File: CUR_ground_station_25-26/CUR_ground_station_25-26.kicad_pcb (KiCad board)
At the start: 2 copper layers, 27 parts, among them J2 UJ20-C-H-G-SMT-P16-TR, Q2 NTR4003N, U1 ESP32-S3-WROOM-1, U2 BQ24232RGT, U3 NCP186AMX330TAG, U4 USBLC6-2SC6, U5 E22-400MM_22S, U6 2.13" Epaper Module

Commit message: started layout-ing
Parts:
- removed D1: CLV1L-FKB-CJQRNQEFGBB79353, LED_SMD:LED_Cree-PLCC4_3.2x2.8mm_CCW
- added BZ1: CMT-1209-390T, Buzzer_SameSky:Buzzer_SameSky_CEM-1203_42, F.Cu at (91.3, 61.9)
- added C1: 10u, Capacitor_SMD:C_0603_1608Metric, F.Cu at (140.7, 89.4)
- added C10: 100n, Capacitor_SMD:C_0603_1608Metric, F.Cu at (55.7, 98.1)
- added C11: 100n, Capacitor_SMD:C_0603_1608Metric, F.Cu at (89.5, 98.6)
- added C12: 22u, Capacitor_SMD:C_0603_1608Metric, F.Cu at (89.4, 95.0)
- added C13: 1u, Capacitor_SMD:C_0603_1608Metric, F.Cu at (66.1, 100.3)
- added C14: DNP, Capacitor_SMD:C_0603_1608Metric, F.Cu at (74.9, 85.3)
- added C15: DNP, Capacitor_SMD:C_0603_1608Metric, F.Cu at (75.2, 82.2)
- added C2: 10u, Capacitor_SMD:C_0603_1608Metric, F.Cu at (97.5, 77.3)
- added C3: 10u, Capacitor_SMD:C_0603_1608Metric, F.Cu at (92.9, 77.2)
- added C4: 10u, Capacitor_SMD:C_0603_1608Metric, F.Cu at (101.6, 88.4)
- added C5: 10u, Capacitor_SMD:C_0603_1608Metric, F.Cu at (101.6, 90.9)
- added J1: Conn_01x02, Connector_JST:JST_PH_B2B-PH-K_1x02_P2.00mm_Vertical, F.Cu at (130.1, 97.7)
- added J3: Conn_Coaxial_Small, Conn_Coaxial_RFSOLUTIONS_CON-SMA-EDGE-S:Conn_Coaxial_RFSOLUTIONS_CON-SMA-EDGE-S, F.Cu at (98.2, 30.5)
- added J4: Conn_01x04_Pin, Connector_PinHeader_2.54mm:PinHeader_1x04_P2.54mm_Vertical, F.Cu at (48.3, 91.5)
- added Q1: NTR4003N, Package_TO_SOT_SMD:SOT-23, F.Cu at (100.5, 57.0)
- added R12: 10k, Resistor_SMD:R_0603_1608Metric, F.Cu at (134.9, 88.9)
- added R13: RC0603FR-071K74L, Resistor_SMD:R_0603_1608Metric, F.Cu at (100.0, 73.2)
- added R14: 10k, Resistor_SMD:R_0603_1608Metric, F.Cu at (105.6, 83.4)
- added R15: 35k, Resistor_SMD:R_0603_1608Metric, F.Cu at (105.6, 85.9)
- added R26: 0, Resistor_SMD:R_0603_1608Metric, F.Cu at (62.3, 101.7)
- added R27: 10k, Resistor_SMD:R_0603_1608Metric, F.Cu at (64.2, 100.3)
- added R28: 0, Resistor_SMD:R_0603_1608Metric, F.Cu at (78.9, 82.8)
- added R29: 0, Resistor_SMD:R_0603_1608Metric, F.Cu at (78.9, 85.3)
- added R33: 270, Resistor_SMD:R_0603_1608Metric, F.Cu at (46.5, 61.1)
- added R34: 47, Resistor_SMD:R_0603_1608Metric, F.Cu at (49.9, 61.1)
- added R35: 47, Resistor_SMD:R_0603_1608Metric, F.Cu at (50.6, 58.4)
- added R36: 270, Resistor_SMD:R_0603_1608Metric, F.Cu at (55.6, 61.1)
- added R37: 47, Resistor_SMD:R_0603_1608Metric, F.Cu at (59.0, 61.1)
- added R38: 47, Resistor_SMD:R_0603_1608Metric, F.Cu at (59.8, 58.3)
- added R4: 10k, Resistor_SMD:R_0603_1608Metric, F.Cu at (100.6, 61.5)
- added R5: 150, Resistor_SMD:R_0603_1608Metric, F.Cu at (100.1, 65.2)
- added SW1: PTS815SJM250SMTRLFS, PTS815_SJM_250_SMTR_LFS:SW_Push_PTS815_SJM_250_SMTR_LFS, F.Cu at (49.8, 76.1)
- added SW2: PTS815SJM250SMTRLFS, PTS815_SJM_250_SMTR_LFS:SW_Push_PTS815_SJM_250_SMTR_LFS, F.Cu at (56.3, 81.0)
- added SW3: PTS815SJM250SMTRLFS, PTS815_SJM_250_SMTR_LFS:SW_Push_PTS815_SJM_250_SMTR_LFS, F.Cu at (56.3, 70.7)
- added SW4: PTS815SJM250SMTRLFS, PTS815_SJM_250_SMTR_LFS:SW_Push_PTS815_SJM_250_SMTR_LFS, F.Cu at (62.6, 76.0)
- added SW5: PTS815SJM250SMTRLFS, PTS815_SJM_250_SMTR_LFS:SW_Push_PTS815_SJM_250_SMTR_LFS, F.Cu at (113.9, 110.7)
- added SW7: PTS815SJM250SMTRLFS, PTS815_SJM_250_SMTR_LFS:SW_Push_PTS815_SJM_250_SMTR_LFS, F.Cu at (96.5, 99.4)
- added SW8: PTS815SJM250SMTRLFS, PTS815_SJM_250_SMTR_LFS:SW_Push_PTS815_SJM_250_SMTR_LFS, F.Cu at (59.9, 98.1)
- added TP1: TestPoint_Small, TestPoint_KOASpeer:TestPoint_Chip_RCUCTE_0603, F.Cu at (89.1, 45.2)
- added TP10: TestPoint_Small, TestPoint_KOASpeer:TestPoint_Chip_RCUCTE_0603, F.Cu at (82.0, 42.7)
- added TP11: TestPoint_Small, TestPoint_KOASpeer:TestPoint_Chip_RCUCTE_0603, F.Cu at (82.0, 40.1)
- added TP12: TestPoint_Small, TestPoint_KOASpeer:TestPoint_Chip_RCUCTE_0603, F.Cu at (111.6, 95.1)
- added TP14: TestPoint_Small, TestPoint_KOASpeer:TestPoint_Chip_RCUCTE_0603, F.Cu at (111.6, 97.7)
- added TP15: TestPoint_Small, TestPoint_KOASpeer:TestPoint_Chip_RCUCTE_0603, F.Cu at (111.6, 100.2)
- added TP16: TestPoint_Small, TestPoint_KOASpeer:TestPoint_Chip_RCUCTE_0603, F.Cu at (111.6, 102.8)
- added TP17: TestPoint_Small, TestPoint_KOASpeer:TestPoint_Chip_RCUCTE_0603, F.Cu at (111.6, 105.3)
- added TP2: TestPoint_Small, TestPoint_KOASpeer:TestPoint_Chip_RCUCTE_0603, F.Cu at (89.1, 42.7)
- added TP3: TestPoint_Small, TestPoint_KOASpeer:TestPoint_Chip_RCUCTE_0603, F.Cu at (89.1, 40.1)
- added TP4: TestPoint_Small, TestPoint_KOASpeer:TestPoint_Chip_RCUCTE_0603, F.Cu at (89.1, 37.6)
- added TP5: TestPoint_Small, TestPoint_KOASpeer:TestPoint_Chip_RCUCTE_0603, F.Cu at (85.5, 45.2)
- added TP6: TestPoint_Small, TestPoint_KOASpeer:TestPoint_Chip_RCUCTE_0603, F.Cu at (85.5, 42.7)
- added TP7: TestPoint_Small, TestPoint_KOASpeer:TestPoint_Chip_RCUCTE_0603, F.Cu at (85.5, 40.1)
- added TP8: TestPoint_Small, TestPoint_KOASpeer:TestPoint_Chip_RCUCTE_0603, F.Cu at (85.5, 37.6)
- added TP9: TestPoint_Small, TestPoint_KOASpeer:TestPoint_Chip_RCUCTE_0603, F.Cu at (82.0, 45.2)
- R16, R17, R18, R19: footprint Resistor_SMD:R_0402_1005Metric -> Resistor_SMD:R_0603_1608Metric
- U1: value ESP32-S3-WROOM-1 -> ESP32-S3-MINI-1; footprint RF_Module:ESP32-S3-WROOM-1 -> RF_Module:ESP32-S2-MINI-1
- U3: footprint Package_DFN_QFN:DFN-6-1EP_1.2x1.2mm_P0.4mm_EP0.3x0.94mm_PullBack -> XDFN8_1P6X1P2_onsemi:XDFN8_1P6X1P2_onsemi
- moved U5 77.1 mm to (97.3, 40.0), turned to 180 degrees
- moved R25 64.8 mm to (105.9, 32.7), turned to 180 degrees
- moved R24 59.8 mm to (105.9, 35.2), turned to 180 degrees
- moved R23 54.8 mm to (105.9, 37.7), turned to 180 degrees
- moved C9 49.8 mm to (105.9, 40.2), turned to 180 degrees
- moved C8 44.8 mm to (105.9, 42.7), turned to 180 degrees
- moved D5 42.6 mm to (104.3, 61.3), turned to 180 degrees
- moved C6 39.8 mm to (105.9, 45.2), turned to 180 degrees
- moved Q2 31.1 mm to (107.4, 105.5)
- moved D4 31.0 mm to (107.4, 100.9)
- moved D2 30.8 mm to (107.4, 96.2)
- moved R18 28.0 mm to (120.1, 104.6)
- moved R17 27.5 mm to (120.1, 102.1)
- moved R16 27.0 mm to (120.1, 99.6)
- moved C7 20.9 mm to (114.8, 98.0)
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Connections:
- Q2 pad 3: /Power/PWR_BTN -> /MCU/PWR_BTN
- R17 pad 1: /Power/PWR_EN -> /MCU/PWR_EN
- R23 pad 2: /Telemetry/~{RF_NSS} -> /MCU/~{RF_NSS}
- R24 pad 1: /Telemetry/RF_TXEN -> /MCU/RF_TXEN
- R24 pad 2: /Telemetry/RF_IO2 -> /MCU/RF_IO2
- U1 pad 10: /MCU/RF_IO2 -> /MCU/BUZZER
- U1 pad 12: /MCU/RF_IO3 -> /MCU/RF_IO2
- U1 pad 13: Net-(U1-USB_D-) -> /MCU/RF_IO3
- U1 pad 14: Net-(U1-USB_D+) -> /MCU/~{RF_NSS}
- U1 pad 15: unconnected-(U1-IO3-Pad15) -> /MCU/RF_MOSI
- U1 pad 16: unconnected-(U1-IO46-Pad16) -> /MCU/RF_SCK
- U1 pad 17: unconnected-(U1-IO9-Pad17) -> /MCU/RF_MISO
- U1 pad 18: /MCU/~{RF_NSS} -> /MCU/RF_BUSY
- U1 pad 19: /MCU/RF_MOSI -> /MCU/~{RF_RESET}
- U1 pad 2: +3V3 -> GND
- U1 pad 20: /MCU/RF_SCK -> /MCU/LED_1_R
- U1 pad 21: /MCU/RF_MISO -> /MCU/LED_1_G
- U1 pad 22: /MCU/RF_BUSY -> /MCU/LED_1_B
- U1 pad 23: /MCU/RF_RXEN -> Net-(U1-USB_D-)
- U1 pad 24: unconnected-(U1-IO47-Pad24) -> Net-(U1-USB_D+)
- U1 pad 25: unconnected-(U1-IO48-Pad25) -> /MCU/RF_RXEN
- U1 pad 27: /MCU/BOOT -> /MCU/BTN_3
- U1 pad 28: unconnected-(U1-IO35-Pad28) -> /MCU/LED_2_R
- U1 pad 29: unconnected-(U1-IO36-Pad29) -> /MCU/LED_2_G
- U1 pad 3: /MCU/EN -> +3V3
- U1 pad 30: unconnected-(U1-IO37-Pad30) -> /MCU/BTN_4
- U1 pad 31: unconnected-(U1-IO38-Pad31) -> /MCU/LED_2_B
- U1 pad 32: unconnected-(U1-IO39-Pad32) -> /MCU/DISP_D/~{C}
- U1 pad 33: unconnected-(U1-IO40-Pad33) -> /MCU/DISP_CS
- U1 pad 34: unconnected-(U1-IO41-Pad34) -> /MCU/DISP_SCL
- U1 pad 35: unconnected-(U1-IO42-Pad35) -> /MCU/DISP_SDA
- U1 pad 36: /MCU/UART_RX -> /MCU/DISP_BUSY
- U1 pad 37: /MCU/UART_TX -> /MCU/DISP_~{RES}
- U1 pad 38: unconnected-(U1-IO2-Pad38) -> /MCU/BTN_1
- U1 pad 39: unconnected-(U1-IO1-Pad39) -> /MCU/UART_TX
- U1 pad 4: /MCU/DISP_D/~{C} -> /MCU/BOOT
- U1 pad 40: GND -> /MCU/UART_RX
- U1 pad 41: GND -> /MCU/BTN_2
- U1 pad 5: /MCU/DISP_CS -> /MCU/~{CHG}
- U1 pad 6: /MCU/DISP_SCL -> /MCU/~{PGOOD}
- U1 pad 7: /MCU/DISP_SDA -> /MCU/BATT_VSENSE
- U1 pad 8: /MCU/DISP_~{RES} -> /MCU/PWR_EN
- U1 pad 9: /MCU/~{RF_RESET} -> /MCU/PWR_BTN
- U2 pad 7: /Power/~{PGOOD} -> /MCU/~{PGOOD}
- U2 pad 9: /Power/~{CHG} -> /MCU/~{CHG}
- U4 pad 4: /Power/USB_D+ -> /MCU/USB_D+
- U4 pad 6: /Power/USB_D- -> /MCU/USB_D-
- U5 pad 10: /Telemetry/RF_RXEN -> /MCU/RF_RXEN
- U5 pad 11: /Telemetry/RF_BUSY -> /MCU/RF_BUSY
- U5 pad 12: /Telemetry/RF_MISO -> /MCU/RF_MISO
- U5 pad 13: /Telemetry/RF_MOSI -> /MCU/RF_MOSI
- U5 pad 14: /Telemetry/~{RF_NSS} -> /MCU/~{RF_NSS}
- U5 pad 15: /Telemetry/RF_SCK -> /MCU/RF_SCK
- U5 pad 18: /Telemetry/RF_IO1 -> /MCU/RF_IO1
- U5 pad 19: /Telemetry/RF_IO2 -> /MCU/RF_IO2
- U5 pad 20: /Telemetry/RF_IO3 -> /MCU/RF_IO3
- U5 pad 3: /Telemetry/~{RF_RESET} -> /MCU/~{RF_RESET}
- U5 pad 9: /Telemetry/RF_TXEN -> /MCU/RF_TXEN
- U6 pad 1: /User Interface/DISP_BUSY -> /MCU/DISP_BUSY
- U6 pad 2: /User Interface/DISP_~{RES} -> /MCU/DISP_~{RES}
- U6 pad 3: /User Interface/DISP_D/~{C} -> /MCU/DISP_D/~{C}
- U6 pad 4: /User Interface/DISP_CS -> /MCU/DISP_CS
- U6 pad 5: /User Interface/DISP_SCL -> /MCU/DISP_SCL
- U6 pad 6: /User Interface/DISP_SDA -> /MCU/DISP_SDA

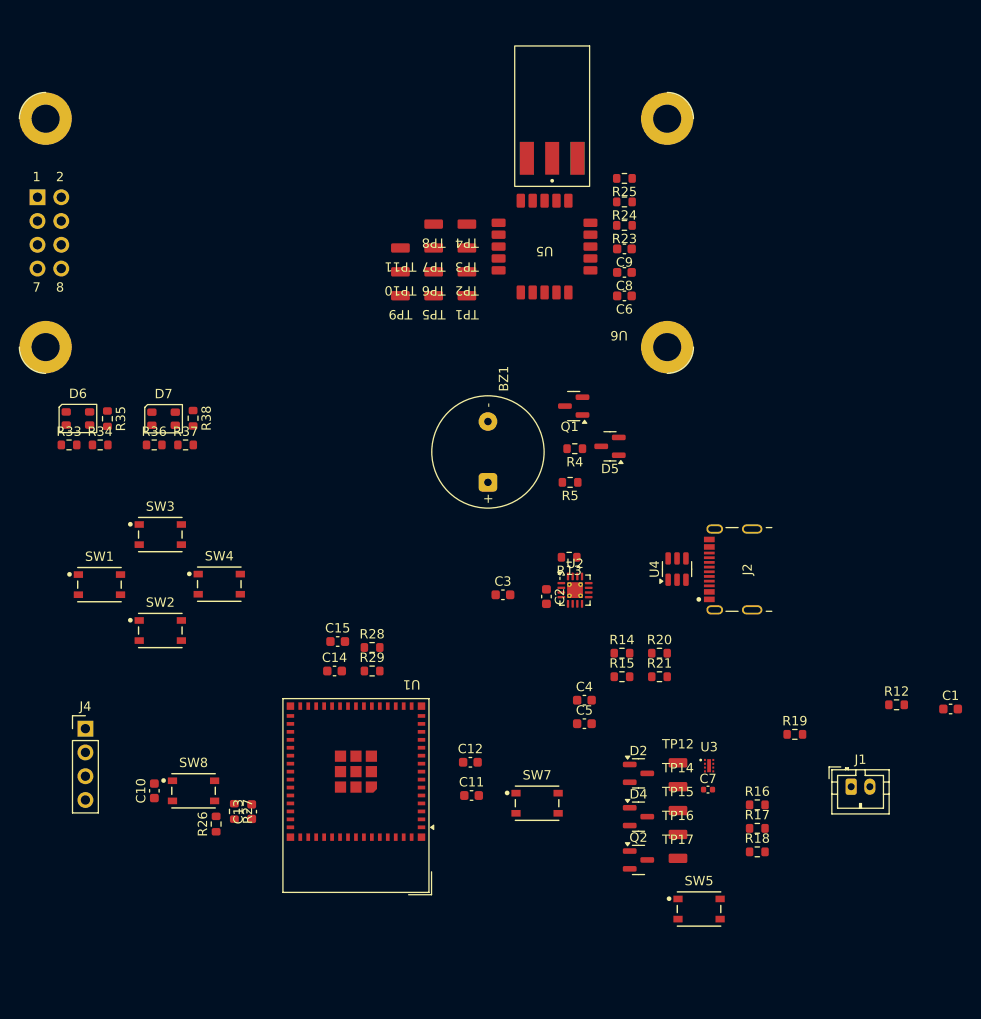
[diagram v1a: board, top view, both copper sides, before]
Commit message: preliminary layout
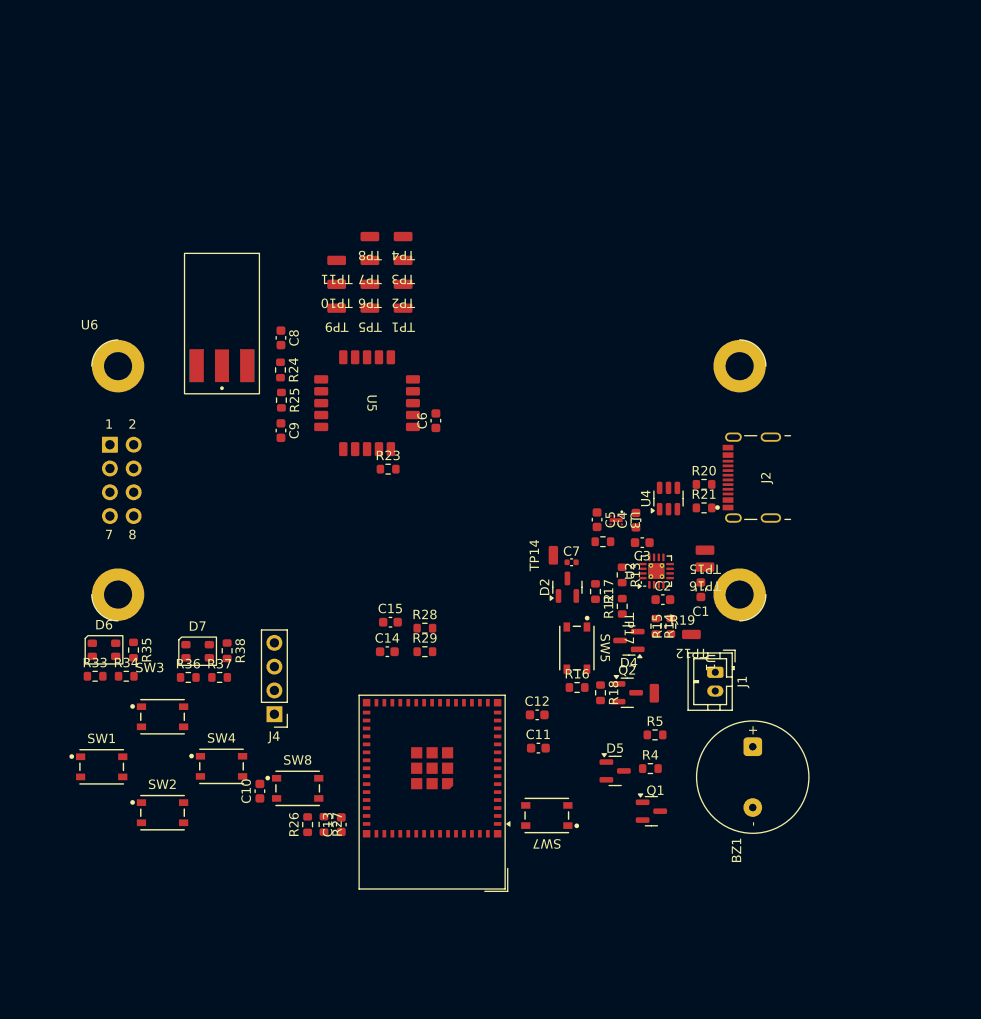
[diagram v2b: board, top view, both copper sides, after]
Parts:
- moved BZ1 44.8 mm to (119.6, 96.6), turned to -90 degrees
- moved Q1 44.1 mm to (108.8, 100.3), turned to 0 degrees
- moved R25 43.6 mm to (69.2, 56.4), turned to -90 degrees
- moved J3 41.7 mm to (62.9, 52.7)
- moved C9 41.5 mm to (69.2, 59.6), turned to -90 degrees
- moved R24 40.9 mm to (69.1, 53.1), turned to -90 degrees
- moved C8 37.4 mm to (69.2, 49.7), turned to -90 degrees
- moved R23 36.3 mm to (80.6, 63.7), turned to 0 degrees
- moved R4 35.1 mm to (108.7, 95.7), turned to 0 degrees
- moved D5 34.7 mm to (104.9, 96.0), turned to 0 degrees
- moved R12 31.1 mm to (105.6, 78.4), turned to 90 degrees
- moved SW5 30.8 mm to (100.8, 82.8), turned to -90 degrees
- moved R17 30.6 mm to (102.8, 76.8), turned to -90 degrees
- moved C1 29.6 mm to (114.0, 76.6), turned to -90 degrees
- moved R19 29.1 mm to (103.6, 71.5), turned to 180 degrees
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
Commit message: Update CUR_ground_station_25-26.kicad_pcb
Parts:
- moved TP4 28.8 mm to (70.4, 65.1), turned to -90 degrees
- moved TP8 28.5 mm to (79.8, 67.4), turned to -90 degrees
- moved TP3 27.2 mm to (74.1, 67.4), turned to -90 degrees
- moved TP7 26.1 mm to (76.0, 67.4), turned to -90 degrees
- moved TP2 23.4 mm to (81.7, 67.4), turned to -90 degrees
- moved TP1 21.3 mm to (78.0, 67.4), turned to 90 degrees
- moved TP5 21.2 mm to (68.4, 65.1), turned to -90 degrees
- moved TP11 17.5 mm to (85.6, 55.5)
- moved TP10 16.9 mm to (85.6, 57.2)
- moved TP9 16.3 mm to (85.6, 59.0)
- moved TP15 11.1 mm to (104.7, 77.6), turned to 0 degrees
- moved J4 10.9 mm to (76.5, 82.5), turned to -90 degrees
- moved R12 10.4 mm to (113.5, 71.6), turned to -90 degrees
- moved TP16 9.92 mm to (104.7, 75.8), turned to 0 degrees
- moved C6 9.68 mm to (79.4, 51.3), turned to 180 degrees
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
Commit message: layout
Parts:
- moved R12 10.2 mm to (104.7, 76.8), turned to 90 degrees
- moved R13 8.93 mm to (104.7, 73.5), turned to -90 degrees
- moved C1 6.52 mm to (111.6, 74.3), turned to -90 degrees
- moved J4 5.89 mm to (70.7, 82.8), turned to 0 degrees
- moved TP12 4.43 mm to (110.2, 84.8)
- moved C2 3.83 mm to (109.1, 76.1), turned to 0 degrees
- moved C10 2.74 mm to (67.8, 100.8), turned to 180 degrees
- moved TP14 2.72 mm to (93.7, 77.1)
- moved C7 2.72 mm to (94.5, 75.1)
- moved D2 2.72 mm to (97.1, 75.5)
- moved R17 2.72 mm to (97.6, 72.6)
- moved TP15 2.72 mm to (102.0, 77.6)
- moved TP16 2.72 mm to (102.0, 75.8)
- moved U2 2.72 mm to (108.4, 73.0), turned to 90 degrees
- moved TP5 2.29 mm to (66.9, 63.4)
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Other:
- board outline added: 74.2 x 53.8 mm

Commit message: Power layout
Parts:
- moved TP17 23.4 mm to (88.1, 77.4), turned to 90 degrees
- moved Q2 18.4 mm to (91.1, 77.2), turned to 180 degrees
- moved R18 14.1 mm to (94.0, 77.2), turned to 90 degrees
- moved C4 13.6 mm to (104.2, 80.3), turned to -90 degrees
- moved R17 11.6 mm to (101.3, 83.5), turned to -90 degrees
- moved C3 11.3 mm to (106.2, 80.3), turned to -90 degrees
- moved R13 11.2 mm to (110.3, 83.2), turned to 0 degrees
- moved U3 10.7 mm to (104.8, 77.0)
- moved C12 10.6 mm to (95.6, 100.5)
- moved R15 10.3 mm to (103.9, 89.8), turned to 0 degrees
- moved R12 9.88 mm to (113.3, 81.7), turned to 180 degrees
- moved SW5 9.85 mm to (109.8, 86.8)
- moved TP12 9.64 mm to (101.4, 88.8), turned to 90 degrees
- moved C5 9.37 mm to (102.0, 75.8)
- moved R16 9.32 mm to (96.6, 77.9), turned to 180 degrees
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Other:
- board size 74.2 x 53.8 mm -> 73.9 x 53.3 mm

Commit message: Update CUR_ground_station_25-26.kicad_pcb
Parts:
- moved R14 5.66 mm to (109.5, 89.2)
- moved R15 5.66 mm to (109.5, 91.0)
- moved TP12 5.66 mm to (107.0, 90.1)
- moved TP15 1.99 mm to (104.8, 72.0)
- moved TP16 1.99 mm to (106.7, 73.5)
- moved R13 1.86 mm to (108.5, 82.6)
- moved R5 1.85 mm to (107.0, 93.7)
- moved SW5 1.15 mm to (108.8, 86.2)
- moved C2 1.10 mm to (111.8, 78.5)
- moved R12 0.96 mm to (112.3, 81.7)
- moved U2 0.94 mm to (108.6, 79.6)
- moved D4 0.82 mm to (114.2, 84.3)
- moved C1 0.82 mm to (110.5, 76.0)
- moved C3 0.81 mm to (105.4, 80.3)
- moved C5 0.81 mm to (101.2, 75.8)
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
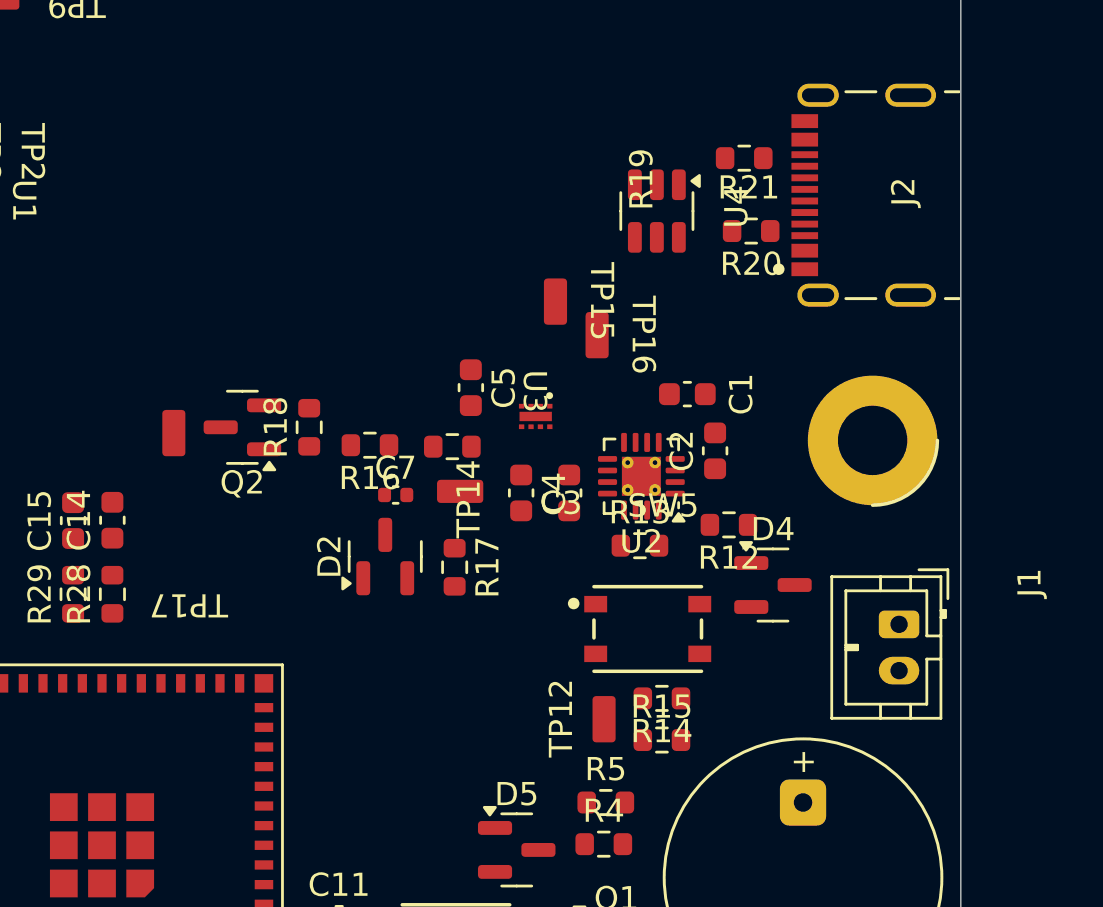
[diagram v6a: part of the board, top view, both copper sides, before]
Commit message: started brief power routing
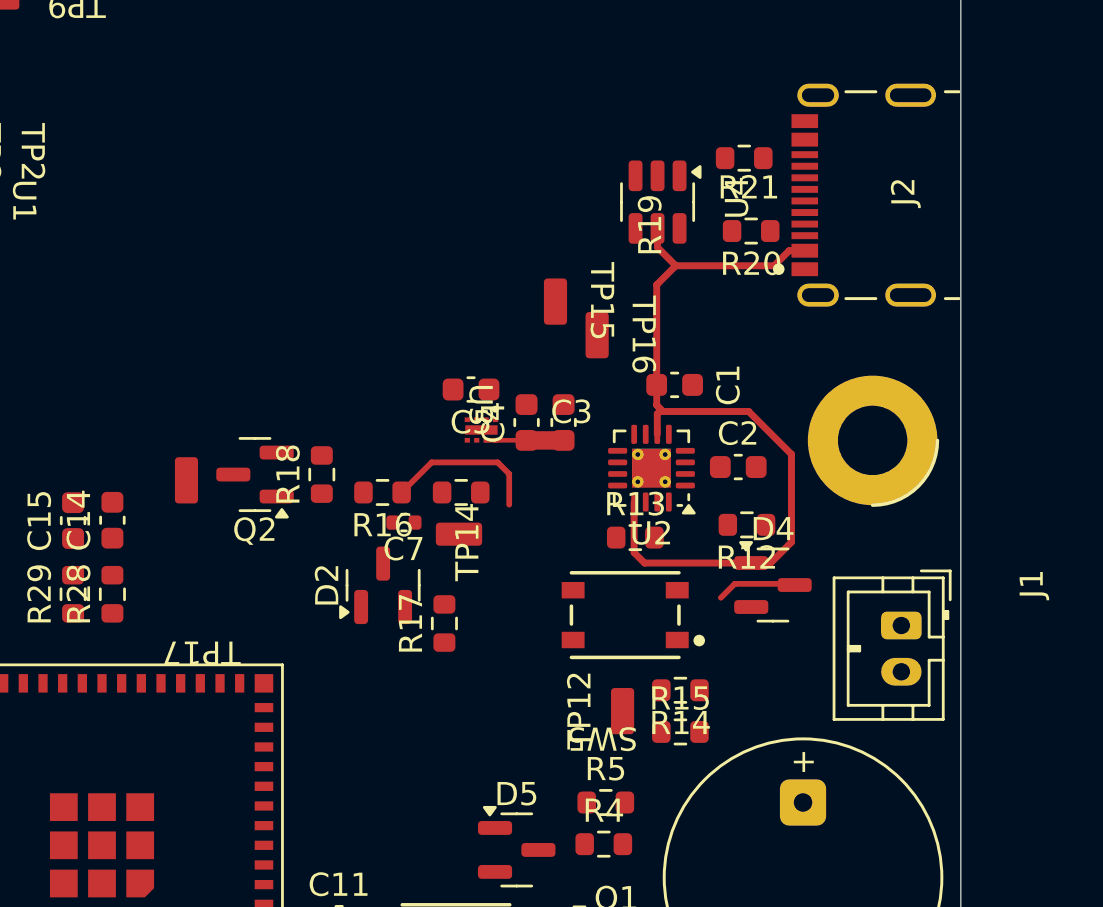
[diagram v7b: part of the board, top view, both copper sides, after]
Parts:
- moved C3 3.05 mm to (105.2, 77.3), turned to 90 degrees
- moved C4 3.05 mm to (103.6, 77.3), turned to 90 degrees
- moved R17 2.47 mm to (100.0, 86.0), turned to 90 degrees
- moved U3 2.42 mm to (101.7, 77.6)
- moved R16 2.11 mm to (97.4, 80.3)
- moved R18 2.11 mm to (94.8, 79.5)
- moved TP17 2.11 mm to (88.9, 79.8)
- moved Q2 2.11 mm to (91.9, 79.5)
- moved R19 2.02 mm to (100.8, 80.3)
- moved TP14 1.85 mm to (100.7, 82.1)
- moved D2 1.25 mm to (97.4, 84.3)
- moved C7 1.24 mm to (98.3, 81.6), turned to 180 degrees
- moved C2 1.22 mm to (112.8, 79.2), turned to 0 degrees
- moved SW5 1.14 mm to (107.9, 85.6), turned to 180 degrees
- moved R14 0.87 mm to (110.2, 88.8)
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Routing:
- net VBUS: track 0.00 -> 35.4 mm
- net Net-(R16-Pad1): track 0.00 -> 6.72 mm
- net Net-(D4-Pad3): track 0.00 -> 3.46 mm
- net IN: track 0.00 -> 3.35 mm
